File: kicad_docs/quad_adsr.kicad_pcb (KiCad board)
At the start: 2 copper layers, 71.1 x 99.1 mm, 155 parts, among them J1 power_in, J10 gate_3_in, J11 trigger_3_in, J12 gate_4_in, J13 trigger_4_in, J14 PJ301M-12, J15 PJ301M-12, J16 PJ301M-12, J17 PJ301M-12, J6 gate_1_i n, J7 trigger_1_in, J8 gate_2_in, J9 trigger_2_in, Q1 MMBT3904, Q10 MMBT3904, Q11 MMBT3904, Q12 MMBT3904, Q2 MMBT3904, Q3 MMBT3904, Q4 MMBT3904, Q5 MMBT3904, Q6 MMBT3904, Q7 MMBT3904, Q8 MMBT3904, Q9 MMBT3904, SW1 Rotary_Encoder_Switch, SW2 Rotary_Encoder_Switch, SW3 Rotary_Encoder_Switch, SW4 Rotary_Encoder_Switch, U1 HDSP-7503, U10 MCP4822, U11 74HC595, U12 74HC595, U2 HDSP-7503, U3 HDSP-7503, U4 HDSP-7503, U5 STM32F103RBTx, U6 LM1117-3.3, U7 TL072, U8 TL072, U9 MCP4822

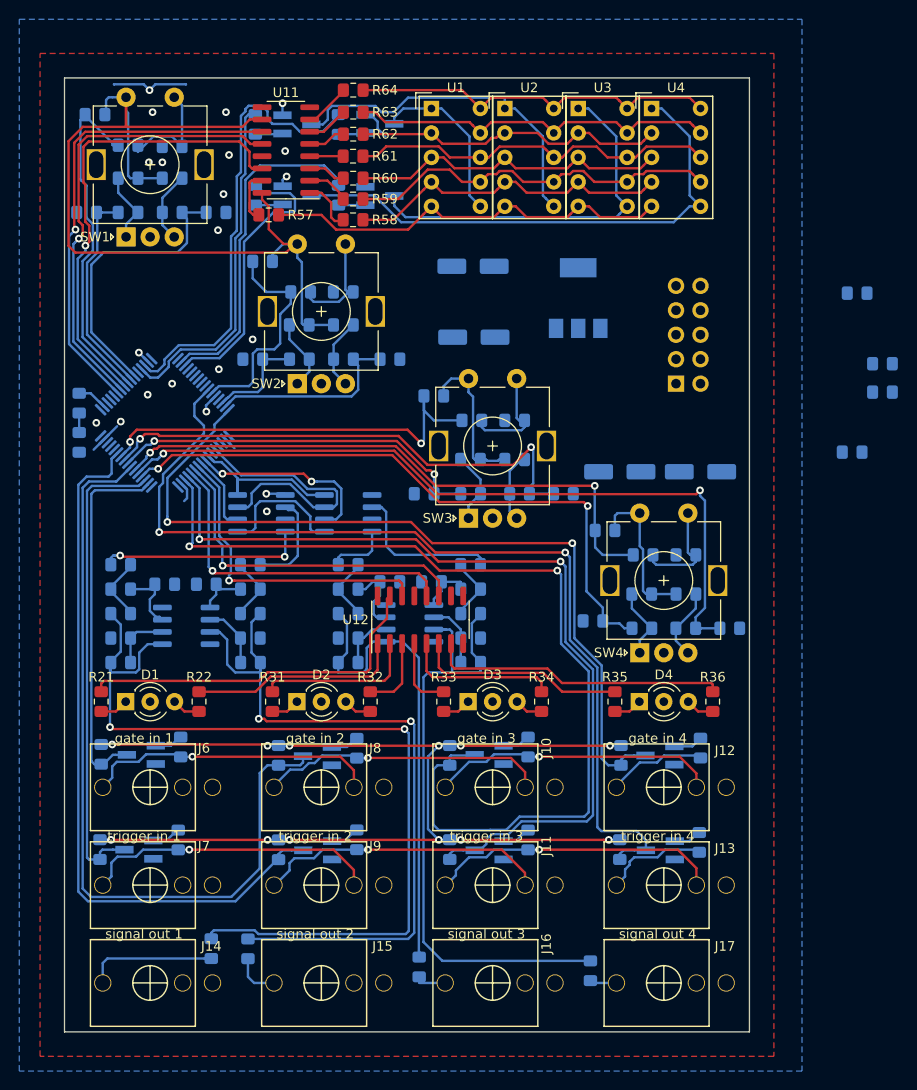
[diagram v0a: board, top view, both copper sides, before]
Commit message: change encoder push-button switch passives
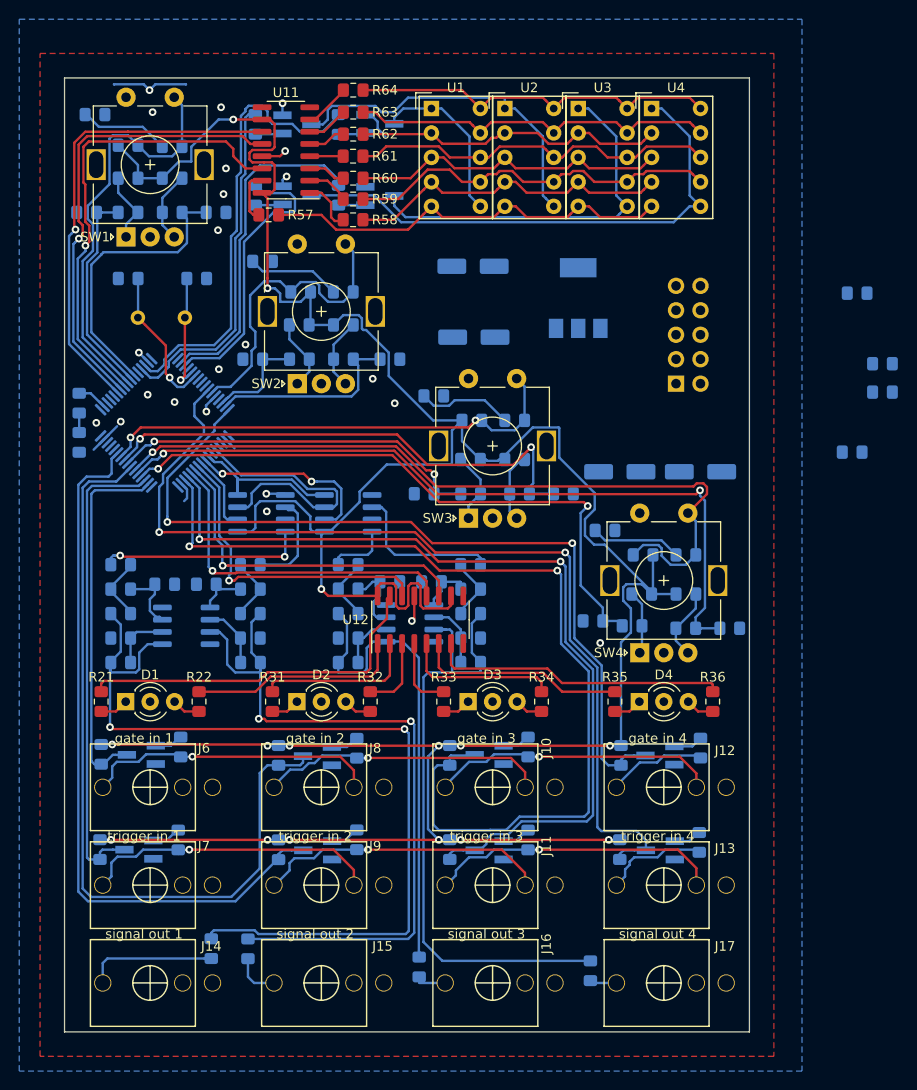
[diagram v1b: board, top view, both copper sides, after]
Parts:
- added C29: 22pF, Capacitor_SMD:C_0805_2012Metric_Pad1.15x1.40mm_HandSolder, B.Cu at (89.9, 71.6)
- added C30: 22pF, Capacitor_SMD:C_0805_2012Metric_Pad1.15x1.40mm_HandSolder, B.Cu at (82.8, 71.6)
- added Y1: 8MHz, Crystal:Crystal_HC49-U_Vertical, B.Cu at (88.7, 75.7)
- C10, C11, C12, C9: value 10nF -> 100nF
- R14, R19, R4, R9: value 10k -> 100
- R27, R28, R29, R30: value 10k -> 4k7
- moved R20 1.05 mm to (135.1, 107.7)
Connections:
- C10 pad 1: /encoders/enc_2_sw_out -> Net-(C10-Pad1)
- C10 pad 2: +3V3 -> GND
- C11 pad 1: /encoders/enc_3_sw_out -> Net-(C11-Pad1)
- C11 pad 2: +3V3 -> GND
- C12 pad 1: /encoders/enc_4_sw_out -> Net-(C12-Pad1)
- C12 pad 2: +3V3 -> GND
- C9 pad 1: /encoders/enc_1_sw_out -> Net-(C9-Pad1)
- C9 pad 2: +3V3 -> GND
- R14 pad 1: Net-(R14-Pad1) -> /encoders/enc_3_sw_out
- R14 pad 2: GND -> Net-(C11-Pad1)
- R19 pad 1: Net-(R19-Pad1) -> /encoders/enc_4_sw_out
- R19 pad 2: GND -> Net-(C12-Pad1)
- R27 pad 1: Net-(R27-Pad1) -> /encoders/enc_1_sw_out
- R27 pad 2: /encoders/enc_1_sw_out -> +3V3
- R28 pad 1: Net-(R28-Pad1) -> +3V3
- R29 pad 1: Net-(R14-Pad1) -> /encoders/enc_3_sw_out
- R29 pad 2: /encoders/enc_3_sw_out -> +3V3
- R30 pad 1: Net-(R19-Pad1) -> +3V3
- R4 pad 1: Net-(R27-Pad1) -> /encoders/enc_1_sw_out
- R4 pad 2: GND -> Net-(C9-Pad1)
- R9 pad 1: Net-(R28-Pad1) -> /encoders/enc_2_sw_out
- R9 pad 2: GND -> Net-(C10-Pad1)
- SW1 pad S1: Net-(R27-Pad1) -> /encoders/enc_1_sw_out
- SW1 pad S2: +3V3 -> GND
- SW2 pad S1: Net-(R28-Pad1) -> /encoders/enc_2_sw_out
- SW2 pad S2: +3V3 -> GND
- SW3 pad S1: Net-(R14-Pad1) -> /encoders/enc_3_sw_out
- SW3 pad S2: +3V3 -> GND
- SW4 pad S1: Net-(R19-Pad1) -> /encoders/enc_4_sw_out
- SW4 pad S2: +3V3 -> GND
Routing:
- net +3V3: track 265.8 -> 325.4 mm, vias 12 -> 15
- net /encoders/enc_4_sw_out: track 61.3 -> 79.3 mm, vias 2 -> 1
- net Net-(C30-Pad1): track 0.00 -> 15.3 mm, vias 0 -> 1
- net Net-(C29-Pad1): track 0.00 -> 12.3 mm, vias 0 -> 1
- net Net-(R27-Pad1): track 12.1 -> 0.00 mm
- net Net-(R28-Pad1): track 11.3 -> 0.00 mm
- net Net-(R14-Pad1): track 11.1 -> 0.00 mm
- net Net-(R19-Pad1): track 11.1 -> 0.00 mm
- net Net-(C11-Pad1): track 0.00 -> 9.93 mm
- net Net-(C10-Pad1): track 0.00 -> 9.70 mm
- net Net-(C12-Pad1): track 0.00 -> 9.45 mm
- net /encoders/enc_2_sw_out: track 23.0 -> 32.2 mm
- net Net-(C9-Pad1): track 0.00 -> 9.15 mm
- net /encoders/enc_1_sw_out: track 36.2 -> 43.3 mm
- net GND: track 26.3 -> 32.0 mm, vias 21 -> 23
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
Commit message: add EEPROM, big pcb re-design
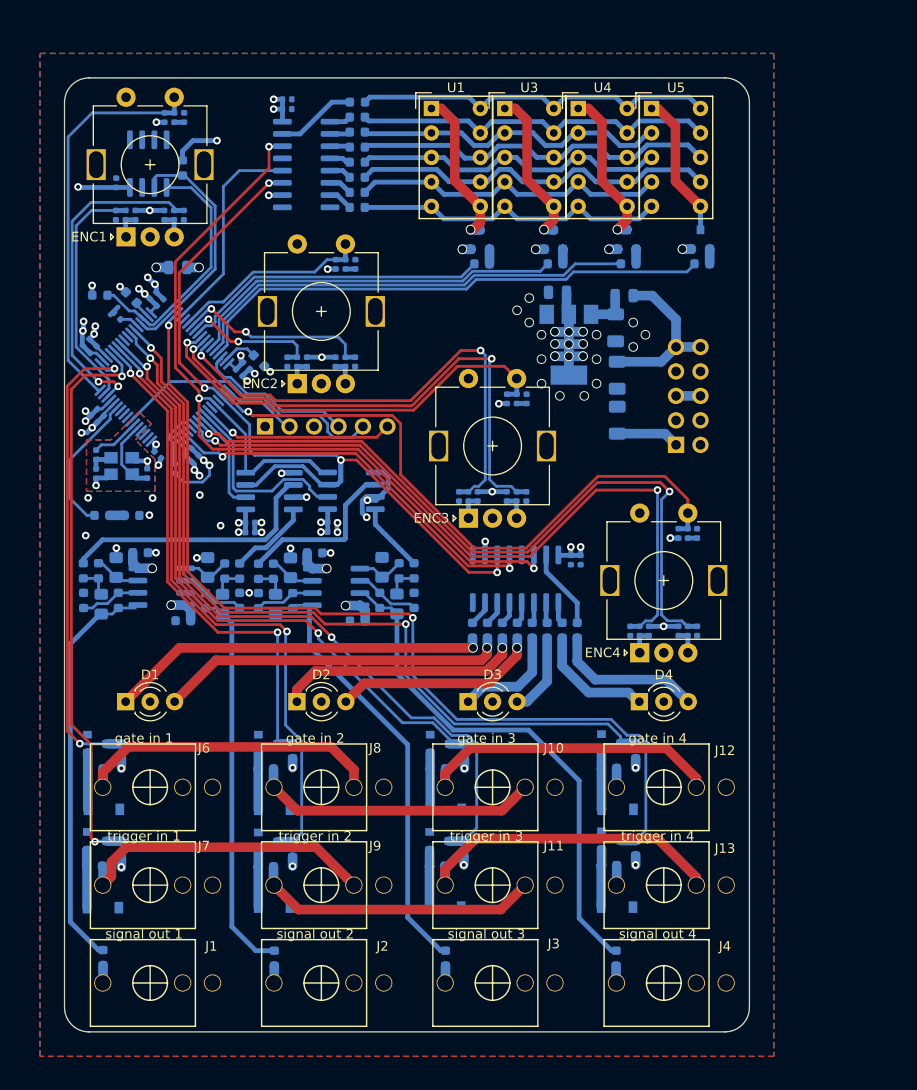
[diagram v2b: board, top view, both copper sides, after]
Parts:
- removed the U5 at (86.6, 86.6)
- removed Y1: 8MHz, Crystal:Crystal_HC49-U_Vertical
- added C31: 100nF, Capacitor_SMD:C_0402_1005Metric, B.Cu at (128.8, 100.9)
- added C32: 100nF, Capacitor_SMD:C_0402_1005Metric, B.Cu at (129.8, 100.9)
- added C33: 100nF, Capacitor_SMD:C_0603_1608Metric, B.Cu at (88.5, 107.2)
- added C34: 100nF, Capacitor_SMD:C_0603_1608Metric, B.Cu at (84.1, 100.1)
- added C35: 100nF, Capacitor_SMD:C_0603_1608Metric, B.Cu at (106.6, 107.2)
- added C36: 100nF, Capacitor_SMD:C_0603_1608Metric, B.Cu at (102.2, 100.1)
- added C37: 2n2, Capacitor_SMD:C_0805_2012Metric_Pad1.15x1.40mm_HandSolder, B.Cu at (99.7, 101.7)
- added C38: 2n2, Capacitor_SMD:C_0805_2012Metric_Pad1.15x1.40mm_HandSolder, B.Cu at (81.6, 101.6)
- added C39: 2n2, Capacitor_SMD:C_0805_2012Metric_Pad1.15x1.40mm_HandSolder, B.Cu at (80.0, 105.4)
- added C40: 2n2, Capacitor_SMD:C_0805_2012Metric_Pad1.15x1.40mm_HandSolder, B.Cu at (98.1, 105.4)
- added C41: 2n2, Capacitor_SMD:C_0805_2012Metric_Pad1.15x1.40mm_HandSolder, B.Cu at (109.2, 101.6)
- added C42: 2n2, Capacitor_SMD:C_0805_2012Metric_Pad1.15x1.40mm_HandSolder, B.Cu at (91.1, 101.6)
- added C43: 2n2, Capacitor_SMD:C_0805_2012Metric_Pad1.15x1.40mm_HandSolder, B.Cu at (92.6, 105.4)
- added C44: 2n2, Capacitor_SMD:C_0805_2012Metric_Pad1.15x1.40mm_HandSolder, B.Cu at (110.7, 105.4)
- added C45: 2.2uF, Capacitor_SMD:C_0603_1608Metric, B.Cu at (83.1, 73.6)
- added C46: 2.2uF, Capacitor_SMD:C_0603_1608Metric, B.Cu at (96.4, 80.2)
- added C47: 12pF, Capacitor_SMD:C_0402_1005Metric, B.Cu at (84.8, 91.9)
- added C48: 12pF, Capacitor_SMD:C_0402_1005Metric, B.Cu at (79.5, 91.9)
- added C49: 100nF, Capacitor_SMD:C_0402_1005Metric, B.Cu at (79.2, 79.0)
- added C50: 100nF, Capacitor_SMD:C_0402_1005Metric, B.Cu at (78.4, 78.3)
- added C51: 10uF, Capacitor_SMD:C_1206_3216Metric, B.Cu at (133.6, 81.7)
- added C52: 10uF, Capacitor_SMD:C_1206_3216Metric, B.Cu at (133.6, 86.3)
- added C53: 100nF, Capacitor_SMD:C_0402_1005Metric, B.Cu at (81.6, 61.7)
- added D10: 1N4148W, Diode_SMD:D_SOD-123, B.Cu at (115.8, 126.7)
- added D11: 1N4148W, Diode_SMD:D_SOD-123, B.Cu at (115.7, 136.9)
- added D12: 1N4148W, Diode_SMD:D_SOD-123, B.Cu at (133.6, 126.7)
- added D13: 1N4148W, Diode_SMD:D_SOD-123, B.Cu at (133.6, 136.9)
- added D6: 1N4148W, Diode_SMD:D_SOD-123, B.Cu at (80.3, 126.7)
- added D7: 1N4148W, Diode_SMD:D_SOD-123, B.Cu at (80.2, 137.0)
- added D8: 1N4148W, Diode_SMD:D_SOD-123, B.Cu at (98.0, 126.7)
- added D9: 1N4148W, Diode_SMD:D_SOD-123, B.Cu at (98.0, 136.9)
- added FB1: Ferrite_Bead_Small, Inductor_SMD:L_0805_2012Metric, B.Cu at (134.3, 73.4)
- added HSE1: 16MHz, Crystal:Crystal_SMD_3225-4Pin_3.2x2.5mm, B.Cu at (82.1, 91.1)
- added J14: SWD_header, Connector_PinHeader_2.54mm:PinHeader_1x06_P2.54mm_Vertical, B.Cu at (97.0, 87.0)
- added R82: 10k, Resistor_SMD:R_0402_1005Metric, B.Cu at (87.7, 91.4)
- added R83: 10k, Resistor_SMD:R_0402_1005Metric, B.Cu at (81.7, 75.5)
- added R84: 100, Resistor_SMD:R_0402_1005Metric, B.Cu at (79.5, 89.9)
- added R85: 4k7, Resistor_SMD:R_0603_1608Metric, B.Cu at (79.9, 73.4)
- added R86: 4k7, Resistor_SMD:R_0603_1608Metric, B.Cu at (88.5, 60.1)
- added U13: 24LC32, Package_SO:SOIC-8_3.9x4.9mm_P1.27mm, B.Cu at (84.9, 59.7)
- added U2: 74HC595, Package_SO:SOIC-16_3.9x9.9mm_P1.27mm, B.Cu at (101.3, 59.8)
- C1, C12, C2, C4, C5, C7, C8, C9: footprint Capacitor_SMD:C_0805_2012Metric_Pad1.15x1.40mm_HandSolder -> Capacitor_SMD:C_0402_1005Metric
- C10, C11: value 100nF -> 10nF; footprint Capacitor_SMD:C_0805_2012Metric_Pad1.15x1.40mm_HandSolder -> Capacitor_SMD:C_0402_1005Metric
- C13: value C -> 10uF; footprint Capacitor_SMD:C_0805_2012Metric_Pad1.15x1.40mm_HandSolder -> Capacitor_SMD:C_1206_3216Metric
- C14: value CP1 -> 10uF; footprint Capacitor_SMD:CP_Elec_5x5.4 -> Capacitor_SMD:C_0805_2012Metric
- C15: value C -> 10uF; footprint Capacitor_SMD:C_0805_2012Metric_Pad1.15x1.40mm_HandSolder -> Capacitor_SMD:C_0805_2012Metric
- C16, C17, C20: value CP1 -> 100nF; footprint Capacitor_SMD:CP_Elec_5x5.4 -> Capacitor_SMD:C_0402_1005Metric
- C18, C19, C21, C22, C23, C24, C25, C26, C27, C28: value C -> 100nF; footprint Capacitor_SMD:C_0805_2012Metric_Pad1.15x1.40mm_HandSolder -> Capacitor_SMD:C_0402_1005Metric
- C29, C30: value 22pF -> 100nF; footprint Capacitor_SMD:C_0805_2012Metric_Pad1.15x1.40mm_HandSolder -> Capacitor_SMD:C_0402_1005Metric
- C3, C6: value 10nF -> 100nF; footprint Capacitor_SMD:C_0805_2012Metric_Pad1.15x1.40mm_HandSolder -> Capacitor_SMD:C_0402_1005Metric
- D5: footprint LED_SMD:LED_0805_2012Metric_Pad1.15x1.40mm_HandSolder -> LED_SMD:LED_0603_1608Metric
- Q1, Q10, Q11, Q12, Q2, Q3, Q4, Q5, Q6, Q7, Q8, Q9: footprint Package_TO_SOT_SMD:SOT-23_Handsoldering -> Package_TO_SOT_SMD:SOT-23
- R1, R10, R13, R15, R16, R2, R20, R3, R7, R8: footprint Resistor_SMD:R_0805_2012Metric_Pad1.15x1.40mm_HandSolder -> Resistor_SMD:R_0402_1005Metric
- R11, R17, R5: value 10k -> 4k7; footprint Resistor_SMD:R_0805_2012Metric_Pad1.15x1.40mm_HandSolder -> Resistor_SMD:R_0402_1005Metric
- R12, R18, R6: value 10k -> 100; footprint Resistor_SMD:R_0805_2012Metric_Pad1.15x1.40mm_HandSolder -> Resistor_SMD:R_0402_1005Metric
- R14, R19, R4, R9: value 100 -> 10k; footprint Resistor_SMD:R_0805_2012Metric_Pad1.15x1.40mm_HandSolder -> Resistor_SMD:R_0402_1005Metric
- R21, R22: value R -> 10k; footprint Resistor_SMD:R_0805_2012Metric_Pad1.15x1.40mm_HandSolder -> Resistor_SMD:R_0402_1005Metric; moved to B.Cu
- R23: value 1k -> 4k7; footprint Resistor_SMD:R_0805_2012Metric_Pad1.15x1.40mm_HandSolder -> Resistor_SMD:R_0402_1005Metric
- R24: value 1k -> 100; footprint Resistor_SMD:R_0805_2012Metric_Pad1.15x1.40mm_HandSolder -> Resistor_SMD:R_0402_1005Metric
- R25: value 1k -> 3k3; footprint Resistor_SMD:R_0805_2012Metric_Pad1.15x1.40mm_HandSolder -> Resistor_SMD:R_0603_1608Metric
- R26, R37, R38, R39, R40: value 1k -> 330; footprint Resistor_SMD:R_0805_2012Metric_Pad1.15x1.40mm_HandSolder -> Resistor_SMD:R_0603_1608Metric
- R27, R28, R29, R30: value 4k7 -> 330; footprint Resistor_SMD:R_0805_2012Metric_Pad1.15x1.40mm_HandSolder -> Resistor_SMD:R_0603_1608Metric
- R31, R32, R33: value R -> 330; footprint Resistor_SMD:R_0805_2012Metric_Pad1.15x1.40mm_HandSolder -> Resistor_SMD:R_0603_1608Metric; moved to B.Cu
- R34, R35, R36: value R -> 3k3; footprint Resistor_SMD:R_0805_2012Metric_Pad1.15x1.40mm_HandSolder -> Resistor_SMD:R_0603_1608Metric; moved to B.Cu
- R41, R43: value 100k -> 330; footprint Resistor_SMD:R_0805_2012Metric_Pad1.15x1.40mm_HandSolder -> Resistor_SMD:R_0603_1608Metric
- R42, R44: value 10k -> 330; footprint Resistor_SMD:R_0805_2012Metric_Pad1.15x1.40mm_HandSolder -> Resistor_SMD:R_0603_1608Metric
- R45, R47: value 100k -> 1k; footprint Resistor_SMD:R_0805_2012Metric_Pad1.15x1.40mm_HandSolder -> Resistor_SMD:R_0603_1608Metric
- R46, R48: value 10k -> 1k; footprint Resistor_SMD:R_0805_2012Metric_Pad1.15x1.40mm_HandSolder -> Resistor_SMD:R_0603_1608Metric
- R49, R50, R51, R52, R53, R54, R55, R56: footprint Resistor_SMD:R_0805_2012Metric_Pad1.15x1.40mm_HandSolder -> Resistor_SMD:R_0603_1608Metric
- R57, R59, R61, R63: value R -> 100k; footprint Resistor_SMD:R_0805_2012Metric_Pad1.15x1.40mm_HandSolder -> Resistor_SMD:R_0603_1608Metric; moved to B.Cu
- R58, R60, R62, R64: value R -> 10k; footprint Resistor_SMD:R_0805_2012Metric_Pad1.15x1.40mm_HandSolder -> Resistor_SMD:R_0603_1608Metric; moved to B.Cu
- R65, R66, R73, R74: value R -> 50k; footprint Resistor_SMD:R_0805_2012Metric_Pad1.15x1.40mm_HandSolder -> Resistor_SMD:R_0603_1608Metric
- R67, R68, R75, R76: value R -> 200k; footprint Resistor_SMD:R_0805_2012Metric_Pad1.15x1.40mm_HandSolder -> Resistor_SMD:R_0603_1608Metric
- R69, R70, R77, R78: value R -> 33k; footprint Resistor_SMD:R_0805_2012Metric_Pad1.15x1.40mm_HandSolder -> Resistor_SMD:R_0603_1608Metric
- R71, R72, R79, R80: value R -> 68k; footprint Resistor_SMD:R_0805_2012Metric_Pad1.15x1.40mm_HandSolder -> Resistor_SMD:R_0603_1608Metric
- R81: value R -> 2k2; footprint Resistor_SMD:R_0805_2012Metric_Pad1.15x1.40mm_HandSolder -> Resistor_SMD:R_0603_1608Metric
- U11: value 74HC595 -> TL072; footprint Package_SO:SOIC-16_3.9x9.9mm_P1.27mm -> Package_SO:SOIC-8_3.9x4.9mm_P1.27mm; moved to B.Cu
- U12: value 74HC595 -> STM32F405RGTx; footprint Package_SO:SOIC-16_3.9x9.9mm_P1.27mm -> Package_QFP:LQFP-64_10x10mm_P0.5mm; moved to B.Cu
- U6: value LM1117-3.3 -> 74HC595; footprint Package_TO_SOT_SMD:SOT-223-3_TabPin2 -> Package_SO:SOIC-16_3.9x9.9mm_P1.27mm
- U7: value TL072 -> AMS1117-3.3; footprint Package_SO:SOIC-8_3.9x4.9mm_P1.27mm -> Package_TO_SOT_SMD:SOT-223-3_TabPin2
- moved R26 93.4 mm to (106.6, 53.3), turned to 180 degrees
- moved R64 84.0 mm to (135.5, 130.8), turned to 90 degrees
- moved R63 82.6 mm to (132.8, 132.6), turned to 0 degrees
- moved C18 80.3 mm to (79.2, 86.2), turned to 315 degrees
- moved C15 73.9 mm to (88.0, 70.5)
- moved C19 73.5 mm to (86.1, 74.1), turned to 45 degrees
- moved R25 73.3 mm to (119.5, 70.1), turned to 180 degrees
- moved R60 70.5 mm to (117.7, 130.8), turned to 90 degrees
- moved R62 70.4 mm to (135.5, 120.7), turned to 90 degrees
- moved R59 69.8 mm to (114.9, 132.7), turned to 0 degrees
- moved R61 68.9 mm to (132.7, 122.5), turned to 0 degrees
- moved R23 64.9 mm to (140.0, 98.1)
- moved R24 62.8 mm to (140.9, 98.1), turned to 270 degrees
- moved C17 62.6 mm to (80.0, 85.5), turned to 315 degrees
- moved R38 61.5 mm to (127.9, 108.2)
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- renumbered SW1 to ENC1, SW2 to ENC2, SW3 to ENC3, SW4 to ENC4, J14 to J1, J15 to J2, J16 to J3, J17 to J4, J1 to J5, U2 to U3, U3 to U4, U4 to U5
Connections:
- C10 pad 1: Net-(C10-Pad1) -> /encoders/enc_4_a_out
- C11 pad 1: Net-(C11-Pad1) -> /encoders/enc_4_b_out
- C13 pad 2: Net-(C13-Pad2) -> GND
- C14 pad 1: Net-(C14-Pad1) -> +3V3
- C14 pad 2: Net-(C14-Pad2) -> GND
- C15 pad 1: Net-(C15-Pad1) -> +3V3
- C15 pad 2: Net-(C15-Pad2) -> GND
- C16 pad 1: Net-(C16-Pad1) -> +3V3
- C16 pad 2: Net-(C16-Pad2) -> GND
- C17 pad 1: Net-(C17-Pad1) -> +3V3
- C17 pad 2: Net-(C17-Pad2) -> GND
- C18 pad 1: Net-(C18-Pad1) -> +3V3
- C18 pad 2: Net-(C18-Pad2) -> GND
- C19 pad 1: Net-(C19-Pad1) -> +3V3
- C19 pad 2: Net-(C19-Pad2) -> GND
- C20 pad 1: Net-(C20-Pad1) -> +3V3
- C20 pad 2: Net-(C20-Pad2) -> GND
- C21 pad 1: Net-(C21-Pad1) -> +3V3
- C22 pad 1: Net-(C22-Pad1) -> +3V3
- C23 pad 1: /spi_dacs_and_level_shifters/10vp_adsr_1_out -> +3V3
- C23 pad 2: Net-(C23-Pad2) -> GND
- C24 pad 1: /spi_dacs_and_level_shifters/10vp_adsr_3_out -> +3V3
- C24 pad 2: Net-(C24-Pad2) -> GND
- C25 pad 1: Net-(C25-Pad1) -> +3V3
- C26 pad 1: Net-(C26-Pad1) -> +3V3
- C27 pad 1: /spi_dacs_and_level_shifters/10vp_adsr_2_out -> +3V3
- C27 pad 2: Net-(C27-Pad2) -> GND
- C28 pad 1: /spi_dacs_and_level_shifters/10vp_adsr_4_out -> +3V3
- C28 pad 2: Net-(C28-Pad2) -> GND
- C29 pad 1: Net-(C29-Pad1) -> +3V3
- C3 pad 1: /encoders/enc_2_a_out -> Net-(C3-Pad1)
- C30 pad 1: Net-(C30-Pad1) -> +3V3
- C4 pad 1: /encoders/enc_2_b_out -> /encoders/enc_2_a_out
- C5 pad 1: /encoders/enc_3_a_out -> /encoders/enc_2_b_out
- C6 pad 1: /encoders/enc_3_b_out -> Net-(C6-Pad1)
- C7 pad 1: /encoders/enc_4_a_out -> /encoders/enc_3_a_out
- C8 pad 1: /encoders/enc_4_b_out -> /encoders/enc_3_b_out
- ENC1 pad A: Net-(R3-Pad2) -> Net-(ENC1-PadA)
- ENC2 pad A: Net-(R10-Pad1) -> Net-(ENC2-PadA)
- ENC2 pad B: Net-(R6-Pad1) -> Net-(ENC2-PadB)
- ENC3 pad A: Net-(R13-Pad2) -> Net-(ENC3-PadA)
- ENC3 pad B: Net-(R11-Pad1) -> Net-(ENC3-PadB)
- ENC4 pad A: Net-(R18-Pad2) -> Net-(ENC4-PadA)
- ENC4 pad B: Net-(R16-Pad1) -> Net-(ENC4-PadB)
- J1 pad 3: Net-(J14-Pad3) -> Net-(J1-Pad3)
- J2 pad 3: Net-(J15-Pad3) -> Net-(J2-Pad3)
- J3 pad 3: Net-(J16-Pad3) -> Net-(J3-Pad3)
- J4 pad 3: Net-(J17-Pad3) -> Net-(J4-Pad3)
- Q10 pad 1: Net-(Q10-Pad1) -> Net-(D11-Pad1)
- Q11 pad 1: Net-(Q11-Pad1) -> Net-(D12-Pad1)
- Q12 pad 1: Net-(Q12-Pad1) -> Net-(D13-Pad1)
- Q5 pad 1: Net-(Q5-Pad1) -> Net-(D6-Pad1)
- Q6 pad 1: Net-(Q6-Pad1) -> Net-(D7-Pad1)
- Q7 pad 1: Net-(Q7-Pad1) -> Net-(D8-Pad1)
- Q8 pad 1: Net-(Q8-Pad1) -> Net-(D9-Pad1)
- Q9 pad 1: Net-(Q9-Pad1) -> Net-(D10-Pad1)
- R10 pad 1: Net-(R10-Pad1) -> Net-(ENC2-PadA)
- R11 pad 1: Net-(R11-Pad1) -> +3V3
- R11 pad 2: /encoders/enc_3_a_out -> /encoders/enc_2_sw_out
- R12 pad 1: +3V3 -> /encoders/enc_2_sw_out
- R12 pad 2: Net-(R11-Pad1) -> Net-(C6-Pad1)
- R13 pad 1: +3V3 -> Net-(ENC3-PadB)
- R13 pad 2: Net-(R13-Pad2) -> /encoders/enc_3_a_out
- R14 pad 1: /encoders/enc_3_sw_out -> +3V3
- R14 pad 2: Net-(C11-Pad1) -> Net-(ENC3-PadB)
- R15 pad 1: Net-(R13-Pad2) -> +3V3
- R15 pad 2: /encoders/enc_3_b_out -> Net-(ENC3-PadA)
- R16 pad 1: Net-(R16-Pad1) -> Net-(ENC3-PadA)
- R16 pad 2: /encoders/enc_4_a_out -> /encoders/enc_3_b_out
- R17 pad 1: +3V3 -> /encoders/enc_3_sw_out
- R17 pad 2: Net-(R16-Pad1) -> +3V3
- R18 pad 1: +3V3 -> /encoders/enc_3_sw_out
- R18 pad 2: Net-(R18-Pad2) -> Net-(C9-Pad1)
- R19 pad 1: /encoders/enc_4_sw_out -> Net-(ENC4-PadB)
- R19 pad 2: Net-(C12-Pad1) -> /encoders/enc_4_a_out
- R20 pad 1: Net-(R18-Pad2) -> +3V3
- R20 pad 2: /encoders/enc_4_b_out -> Net-(ENC4-PadB)
- R21 pad 1: Net-(D1-Pad1) -> +3V3
- R21 pad 2: /leds/QA -> Net-(ENC4-PadA)
- R22 pad 1: Net-(D1-Pad3) -> Net-(ENC4-PadA)
- R22 pad 2: /leds/QB -> /encoders/enc_4_b_out
- R23 pad 1: Net-(J14-Pad3) -> +3V3
- R23 pad 2: /spi_dacs_and_level_shifters/10vp_adsr_1_out -> /encoders/enc_4_sw_out
- R24 pad 1: Net-(J15-Pad3) -> /encoders/enc_4_sw_out
- R24 pad 2: /spi_dacs_and_level_shifters/10vp_adsr_2_out -> Net-(C12-Pad1)
- R25 pad 1: Net-(J16-Pad3) -> Net-(Q1-Pad1)
- R25 pad 2: /spi_dacs_and_level_shifters/10vp_adsr_3_out -> /seven_segment_display/digit_1_in
- R26 pad 1: Net-(J17-Pad3) -> /seven_segment_display/segment_A
- R26 pad 2: /spi_dacs_and_level_shifters/10vp_adsr_4_out -> Net-(R26-Pad2)
- R27 pad 1: /encoders/enc_1_sw_out -> /seven_segment_display/segment_B
- R27 pad 2: +3V3 -> Net-(R27-Pad2)
- R28 pad 1: +3V3 -> /seven_segment_display/segment_F
- R28 pad 2: /encoders/enc_2_sw_out -> Net-(R28-Pad2)
- R29 pad 1: /encoders/enc_3_sw_out -> /seven_segment_display/segment_C
- R29 pad 2: +3V3 -> Net-(R29-Pad2)
- R3 pad 2: Net-(R3-Pad2) -> Net-(ENC1-PadA)
- R30 pad 1: +3V3 -> /seven_segment_display/segment_G
- R30 pad 2: /encoders/enc_4_sw_out -> Net-(R30-Pad2)
- R31 pad 1: Net-(D2-Pad1) -> /seven_segment_display/segment_DP
- R31 pad 2: /leds/QC -> Net-(R31-Pad2)
- R32 pad 1: Net-(D2-Pad3) -> /seven_segment_display/segment_E
- R32 pad 2: /leds/QD -> Net-(R32-Pad2)
- R33 pad 1: Net-(D3-Pad1) -> /seven_segment_display/segment_D
- R33 pad 2: /leds/QE -> Net-(R33-Pad2)
- R34 pad 1: Net-(D3-Pad3) -> Net-(Q2-Pad1)
- R34 pad 2: /leds/QF -> /seven_segment_display/digit_2_in
- R35 pad 1: Net-(D4-Pad1) -> Net-(Q3-Pad1)
- R35 pad 2: /leds/QG -> /seven_segment_display/digit_3_in
- R36 pad 1: Net-(D4-Pad3) -> Net-(Q4-Pad1)
- R36 pad 2: /leds/QH -> /seven_segment_display/digit_4_in
- R37 pad 1: Net-(Q1-Pad1) -> Net-(D4-Pad3)
- R37 pad 2: /seven_segment_display/digit_1_in -> /leds/QA
- R38 pad 1: Net-(Q2-Pad1) -> Net-(D4-Pad1)
- R38 pad 2: /seven_segment_display/digit_2_in -> /leds/QB
- R39 pad 1: Net-(Q3-Pad1) -> Net-(D3-Pad3)
- R39 pad 2: /seven_segment_display/digit_3_in -> /leds/QC
- R4 pad 1: /encoders/enc_1_sw_out -> Net-(ENC1-PadA)
- R4 pad 2: Net-(C9-Pad1) -> /encoders/enc_1_b_out
- R40 pad 1: Net-(Q4-Pad1) -> Net-(D3-Pad1)
- R40 pad 2: /seven_segment_display/digit_4_in -> /leds/QD
- R41 pad 1: Net-(Q5-Pad1) -> Net-(D2-Pad3)
- R41 pad 2: Net-(J6-Pad3) -> /leds/QE
- R42 pad 1: +3V3 -> Net-(D2-Pad1)
- R42 pad 2: /stmf32/gate_1_in -> /leds/QF
- R43 pad 1: Net-(Q6-Pad1) -> Net-(D1-Pad3)
- R43 pad 2: Net-(J7-Pad3) -> /leds/QG
- R44 pad 1: +3V3 -> Net-(D1-Pad1)
- R44 pad 2: /stmf32/trigger_1_in -> /leds/QH
- R45 pad 1: Net-(Q7-Pad1) -> Net-(J1-Pad3)
- R45 pad 2: /input_jacks/g_2_normalization -> /spi_dacs_and_level_shifters/10vp_adsr_1_out
- R46 pad 1: +3V3 -> Net-(J2-Pad3)
- R46 pad 2: /stmf32/gate_2_in -> /spi_dacs_and_level_shifters/10vp_adsr_2_out
- R47 pad 1: Net-(Q8-Pad1) -> Net-(J3-Pad3)
- R47 pad 2: /input_jacks/t_2_normalization -> /spi_dacs_and_level_shifters/10vp_adsr_3_out
- R48 pad 1: +3V3 -> Net-(J4-Pad3)
- R48 pad 2: /stmf32/trigger_2_in -> /spi_dacs_and_level_shifters/10vp_adsr_4_out
- R49 pad 1: Net-(Q9-Pad1) -> Net-(D6-Pad1)
- R49 pad 2: Net-(J10-Pad3) -> Net-(J6-Pad3)
- R5 pad 1: Net-(R3-Pad2) -> /encoders/enc_1_sw_out
- R5 pad 2: /encoders/enc_1_b_out -> +3V3
- R50 pad 2: /stmf32/gate_3_in -> /stmf32/gate_1_in
- R51 pad 1: Net-(Q10-Pad1) -> Net-(D7-Pad1)
- R51 pad 2: Net-(J11-Pad3) -> Net-(J7-Pad3)
- R52 pad 2: /stmf32/trigger_3_in -> /stmf32/trigger_1_in
- R53 pad 1: Net-(Q11-Pad1) -> Net-(D8-Pad1)
- R53 pad 2: Net-(J12-Pad3) -> /input_jacks/g_2_normalization
- R54 pad 2: /stmf32/gate_4_in -> /stmf32/gate_2_in
- R55 pad 1: Net-(Q12-Pad1) -> Net-(D9-Pad1)
- R55 pad 2: Net-(J13-Pad3) -> /input_jacks/t_2_normalization
- R56 pad 2: /stmf32/trigger_4_in -> /stmf32/trigger_2_in
- R57 pad 1: /seven_segment_display/segment_D -> Net-(D10-Pad1)
- R57 pad 2: Net-(R57-Pad2) -> Net-(J10-Pad3)
- R58 pad 1: /seven_segment_display/segment_E -> +3V3
- R58 pad 2: Net-(R58-Pad2) -> /stmf32/gate_3_in
- R59 pad 1: /seven_segment_display/segment_DP -> Net-(D11-Pad1)
- R59 pad 2: Net-(R59-Pad2) -> Net-(J11-Pad3)
- R6 pad 1: Net-(R6-Pad1) -> /encoders/enc_1_sw_out
- R6 pad 2: /encoders/enc_2_a_out -> Net-(C3-Pad1)
- R60 pad 1: /seven_segment_display/segment_G -> +3V3
- R60 pad 2: Net-(R60-Pad2) -> /stmf32/trigger_3_in
- R61 pad 1: /seven_segment_display/segment_C -> Net-(D12-Pad1)
- R61 pad 2: Net-(R61-Pad2) -> Net-(J12-Pad3)
- R62 pad 1: /seven_segment_display/segment_F -> +3V3
- R62 pad 2: Net-(R62-Pad2) -> /stmf32/gate_4_in
- R63 pad 1: /seven_segment_display/segment_B -> Net-(D13-Pad1)
- R63 pad 2: Net-(R63-Pad2) -> Net-(J13-Pad3)
- R64 pad 1: /seven_segment_display/segment_A -> +3V3
- R64 pad 2: Net-(R64-Pad2) -> /stmf32/trigger_4_in
- R65 pad 1: Net-(C23-Pad2) -> Net-(C40-Pad2)
- R65 pad 2: /spi_dacs_and_level_shifters/adsr_1_3.3v -> /spi_dacs_and_level_shifters/adsr_3_3.3v
- R66 pad 1: Net-(C24-Pad2) -> Net-(C39-Pad2)
- R66 pad 2: /spi_dacs_and_level_shifters/adsr_3_3.3v -> /spi_dacs_and_level_shifters/adsr_1_3.3v
- R67 pad 1: Net-(C21-Pad1) -> Net-(C37-Pad1)
- R67 pad 2: Net-(C23-Pad2) -> Net-(C40-Pad2)
- R68 pad 1: Net-(C22-Pad1) -> Net-(C38-Pad1)
- R68 pad 2: Net-(C24-Pad2) -> Net-(C39-Pad2)
- R7 pad 1: +3V3 -> Net-(ENC2-PadB)
- R7 pad 2: Net-(R6-Pad1) -> /encoders/enc_2_a_out
- R73 pad 1: Net-(C27-Pad2) -> Net-(C44-Pad2)
- R73 pad 2: /spi_dacs_and_level_shifters/adsr_2_3.3v -> /spi_dacs_and_level_shifters/adsr_4_3.3v
- R74 pad 1: Net-(C28-Pad2) -> Net-(C43-Pad2)
- R74 pad 2: /spi_dacs_and_level_shifters/adsr_4_3.3v -> /spi_dacs_and_level_shifters/adsr_2_3.3v
- R75 pad 1: Net-(C25-Pad1) -> Net-(C41-Pad1)
- R75 pad 2: Net-(C27-Pad2) -> Net-(C44-Pad2)
- R76 pad 1: Net-(C26-Pad1) -> Net-(C42-Pad1)
- R76 pad 2: Net-(C28-Pad2) -> Net-(C43-Pad2)
- R8 pad 2: Net-(R10-Pad1) -> Net-(ENC2-PadB)
- R9 pad 1: /encoders/enc_2_sw_out -> +3V3
- R9 pad 2: Net-(C10-Pad1) -> Net-(ENC2-PadA)
- U10 pad 2: /spi_dacs_and_level_shifters/spi_cs_2_in -> /spi_dacs_and_level_shifters/spi_dac2_cs
- U10 pad 3: /spi_dacs_and_level_shifters/spi_clk_in -> /leds/spi_clk_in
- U10 pad 4: /spi_dacs_and_level_shifters/spi_data_in -> /leds/spi_data_in
- U10 pad 6: /spi_dacs_and_level_shifters/adsr_4_3.3v -> /spi_dacs_and_level_shifters/adsr_3_3.3v
- U10 pad 8: /spi_dacs_and_level_shifters/adsr_3_3.3v -> /spi_dacs_and_level_shifters/adsr_4_3.3v
- U11 pad 1: Net-(R58-Pad2) -> /spi_dacs_and_level_shifters/10vp_adsr_3_out
- U11 pad 2: Net-(R59-Pad2) -> Net-(R70-Pad2)
- U11 pad 3: Net-(R60-Pad2) -> Net-(C37-Pad1)
- U11 pad 4: Net-(R61-Pad2) -> -12V
- U11 pad 5: Net-(R62-Pad2) -> Net-(C41-Pad1)
- U11 pad 6: Net-(R63-Pad2) -> Net-(R78-Pad2)
- U11 pad 7: Net-(R64-Pad2) -> /spi_dacs_and_level_shifters/10vp_adsr_4_out
- U11 pad 8: GND -> +12V
- U12 pad 1: /leds/QB -> +3V3
- U12 pad 10: +3V3 -> Net-(U12-Pad10)
- U12 pad 11: /leds/rg_leds_clk_in -> /stmf32/status_led
- U12 pad 12: /leds/rg_leds_en_in -> GND
- U12 pad 13: GND -> +3V3
- U12 pad 14: /leds/rg_leds_data_in -> /encoders/enc_1_a_out
- U12 pad 15: /leds/QA -> /encoders/enc_1_b_out
- U12 pad 16: +3V3 -> /encoders/enc_1_sw_out
- U12 pad 2: /leds/QC -> Net-(U12-Pad2)
- U12 pad 3: /leds/QD -> Net-(U12-Pad3)
- U12 pad 4: /leds/QE -> Net-(U12-Pad4)
- U12 pad 5: /leds/QF -> /stmf32/PHO
- U12 pad 6: /leds/QG -> /stmf32/PH1
- U12 pad 7: /leds/QH -> /stmf32/NRST
- U12 pad 8: GND -> Net-(U12-Pad8)
- U6 pad 1: Net-(U6-Pad1) -> /leds/QB
- U6 pad 2: Net-(U6-Pad2) -> /leds/QC
- U6 pad 3: Net-(U6-Pad3) -> /leds/QD
- U7 pad 1: /spi_dacs_and_level_shifters/10vp_adsr_1_out -> GND
- U7 pad 2: Net-(R69-Pad2) -> +3V3
- U7 pad 3: Net-(C21-Pad1) -> Net-(C13-Pad1)
- U8 pad 1: /spi_dacs_and_level_shifters/10vp_adsr_3_out -> /spi_dacs_and_level_shifters/10vp_adsr_1_out
- U8 pad 2: Net-(R70-Pad2) -> Net-(R69-Pad2)
- U8 pad 3: Net-(C22-Pad1) -> Net-(C38-Pad1)
- U8 pad 5: Net-(C26-Pad1) -> Net-(C42-Pad1)
- U8 pad 6: Net-(R78-Pad2) -> Net-(R77-Pad2)
- U8 pad 7: /spi_dacs_and_level_shifters/10vp_adsr_4_out -> /spi_dacs_and_level_shifters/10vp_adsr_2_out
- U9 pad 2: /spi_dacs_and_level_shifters/spi_cs_1_in -> /spi_dacs_and_level_shifters/spi_dac1_cs
- U9 pad 3: /spi_dacs_and_level_shifters/spi_clk_in -> /leds/spi_clk_in
- U9 pad 4: /spi_dacs_and_level_shifters/spi_data_in -> /leds/spi_data_in
- U9 pad 6: /spi_dacs_and_level_shifters/adsr_2_3.3v -> /spi_dacs_and_level_shifters/adsr_1_3.3v
- U9 pad 8: /spi_dacs_and_level_shifters/adsr_1_3.3v -> /spi_dacs_and_level_shifters/adsr_2_3.3v
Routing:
- net +3V3: track 325.4 -> 93.4 mm, vias 15 -> 49
- net +12V: track 0.00 -> 106.3 mm, vias 0 -> 2
- net /leds/spi_data_in: track 0.00 -> 98.2 mm, vias 0 -> 3
- net /leds/spi_clk_in: track 0.00 -> 85.7 mm, vias 0 -> 4
- net -12V: track 0.00 -> 85.7 mm, vias 0 -> 2
- net /spi_dacs_and_level_shifters/10vp_adsr_1_out: track 94.6 -> 42.2 mm, vias 2 -> 0
- net /seven_segment_display/seven_segment_clk_in: track 48.3 -> 0.00 mm, vias 1 -> 0
- net /seven_segment_display/seven_segment_data_in: track 48.0 -> 0.00 mm, vias 1 -> 0
- net /seven_segment_display/seven_segment_en_in: track 47.8 -> 0.00 mm, vias 1 -> 0
- net GND: track 32.0 -> 77.9 mm, vias 23 -> 54
- net /leds/spi_rg_leds_cs: track 0.00 -> 41.2 mm, vias 0 -> 2
- net Net-(Q4-Pad3): track 55.1 -> 15.1 mm
- net /stmf32/gate_3_in: track 101.3 -> 64.7 mm
- net Net-(D1-Pad1): track 2.96 -> 39.4 mm, vias 0 -> 1
- net /leds/rg_leds_clk_in: track 35.8 -> 0.00 mm, vias 1 -> 0
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- added copper zone on 3.3v, net +3V3
- added copper zone on GND, net GND
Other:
- outline, holes or cut-outs redrawn
- copper layers 2 -> 4
- net class Default: clearance 0.2 -> 0.127
- rule trace_clearance: 0.2 -> 0.127
- board text added: "+12"
- board text added: "-12"
- board text added: "3.3"
- board text added: "DC in"
- board text added: "SWD"
- board text added: "gnd"
- board text added: "nrst"
- board text added: "swclk"
- board text added: "swdio"
- board text added: "swo"

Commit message: spread out 1/8" jacks
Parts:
- moved C6 4.79 mm to (110.2, 67.3)
- moved R12 4.59 mm to (109.0, 67.3)
- moved R11 4.39 mm to (107.7, 67.3)
- moved D2 3.81 mm to (100.3, 111.8)
- moved J10 2.54 mm to (120.5, 121.9)
- moved J3 2.54 mm to (120.5, 147.3)
- moved D1 2.54 mm to (82.5, 113.0)
- moved D3 2.54 mm to (118.1, 113.0)
- moved D4 2.54 mm to (135.9, 113.0)
- moved J1 2.54 mm to (85.1, 147.3)
- moved J12 2.54 mm to (138.4, 121.9)
- moved J2 2.54 mm to (102.9, 147.3)
- moved J4 2.54 mm to (138.4, 147.3)
- moved J6 2.54 mm to (85.1, 121.9)
- moved J8 2.54 mm to (102.9, 121.9)
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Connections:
- ENC1 pad MP: (no net) -> GND
- ENC2 pad MP: (no net) -> GND
- ENC3 pad MP: (no net) -> GND
- ENC4 pad MP: (no net) -> GND
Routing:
- net /encoders/enc_3_b_out: track 51.6 -> 39.0 mm
- net /encoders/enc_4_b_out: track 73.2 -> 60.6 mm
- net +3V3: track 93.4 -> 104.2 mm
- net /encoders/enc_3_a_out: track 54.5 -> 45.1 mm
- net /encoders/enc_4_a_out: track 75.5 -> 66.5 mm
- net /input_jacks/g_2_normalization: track 30.0 -> 35.4 mm
- net /spi_dacs_and_level_shifters/10vp_adsr_4_out: track 54.0 -> 49.4 mm
- net GND: track 77.9 -> 73.3 mm, vias 54 -> 52
- net /encoders/enc_2_sw_out: track 20.7 -> 24.4 mm
- net Net-(D3-Pad3): track 8.51 -> 5.37 mm
- net Net-(D4-Pad1): track 12.5 -> 9.70 mm
- net /encoders/enc_3_sw_out: track 44.8 -> 47.6 mm
- net Net-(J4-Pad3): track 1.79 -> 4.33 mm
- net Net-(J2-Pad3): track 1.79 -> 4.33 mm
- net Net-(J1-Pad3): track 1.85 -> 4.39 mm
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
